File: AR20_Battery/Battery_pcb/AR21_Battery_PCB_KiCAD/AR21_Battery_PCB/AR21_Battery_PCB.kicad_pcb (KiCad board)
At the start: 2 copper layers, 109 x 52 mm, 4 parts, among them J1 Conn_01x01_Female, J2 Conn_01x01_Male, J3 Conn_01x01_Male, J4 Conn_01x01_Female

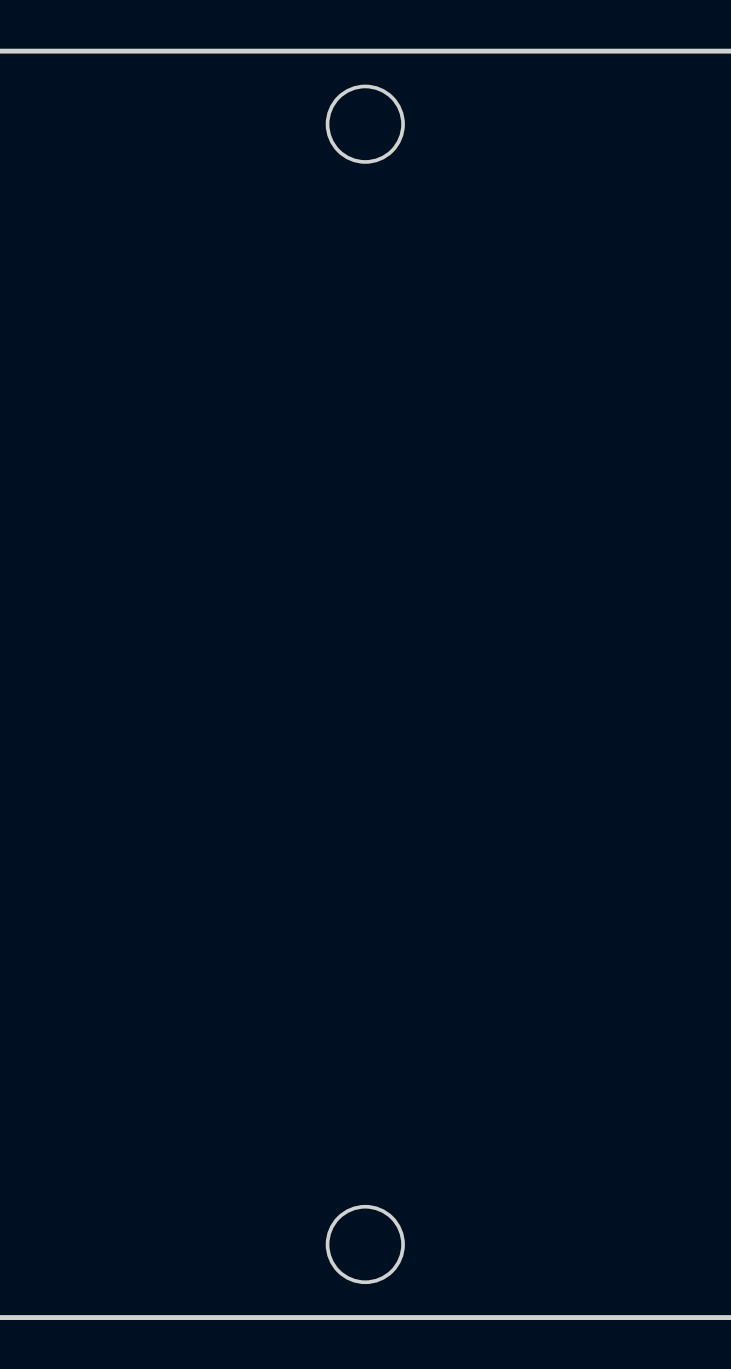
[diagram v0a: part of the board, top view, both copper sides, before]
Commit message: Fixed: Mounting holes
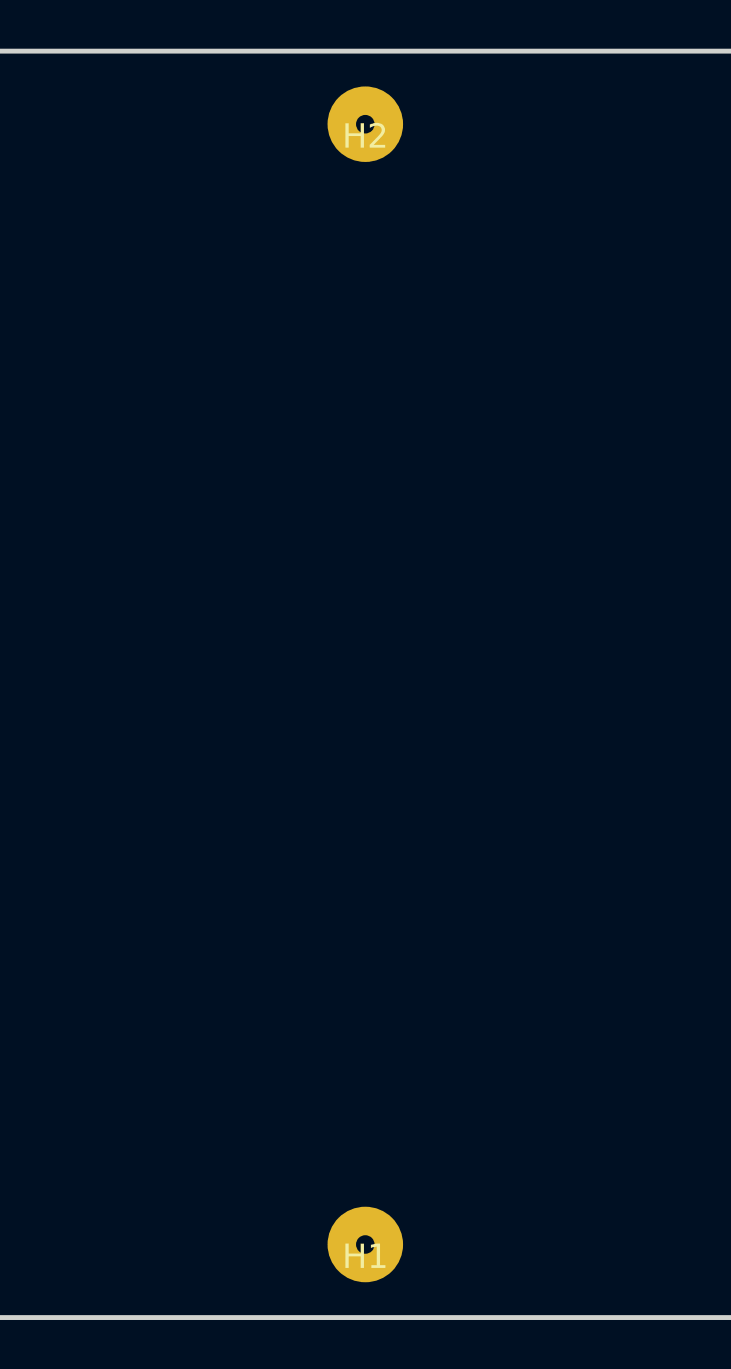
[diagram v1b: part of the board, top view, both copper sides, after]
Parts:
- added H1: MountingHole, AR21_Battery_lib:M3 hole, F.Cu at (140.5, 125.1)
- added H2: MountingHole, AR21_Battery_lib:M3 hole, F.Cu at (140.5, 79.1)
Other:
- outline, holes or cut-outs redrawn
